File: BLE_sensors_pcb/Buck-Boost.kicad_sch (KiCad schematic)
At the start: 6 parts, among them U3 TPS63031DSK

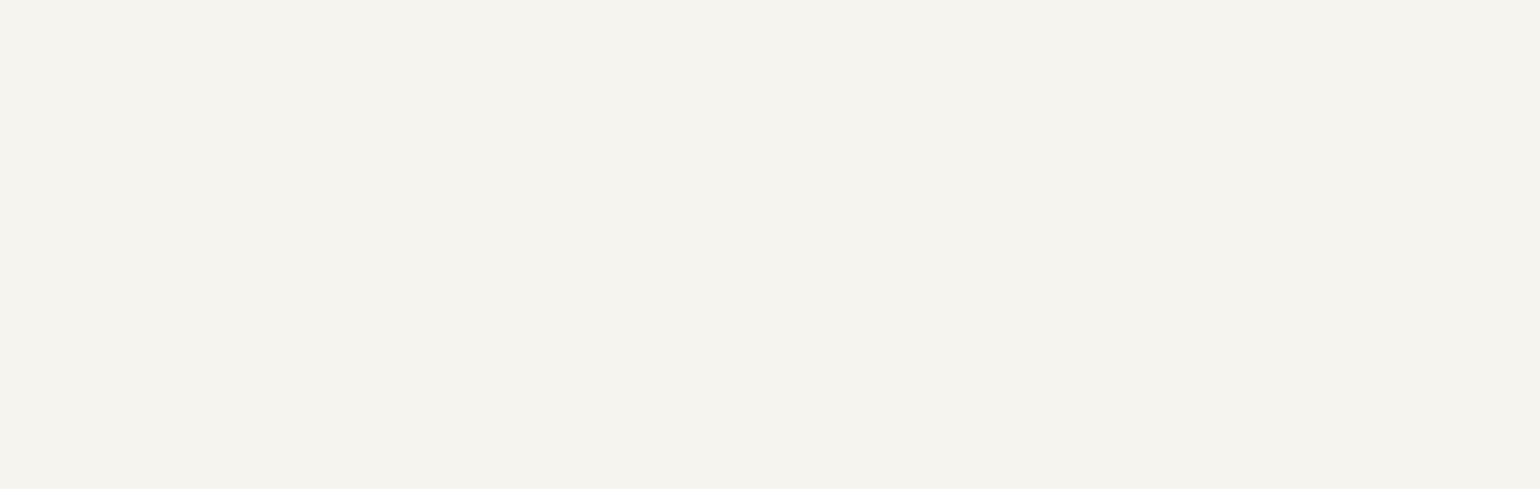
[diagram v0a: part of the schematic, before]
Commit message: Footprints and some pcb placement
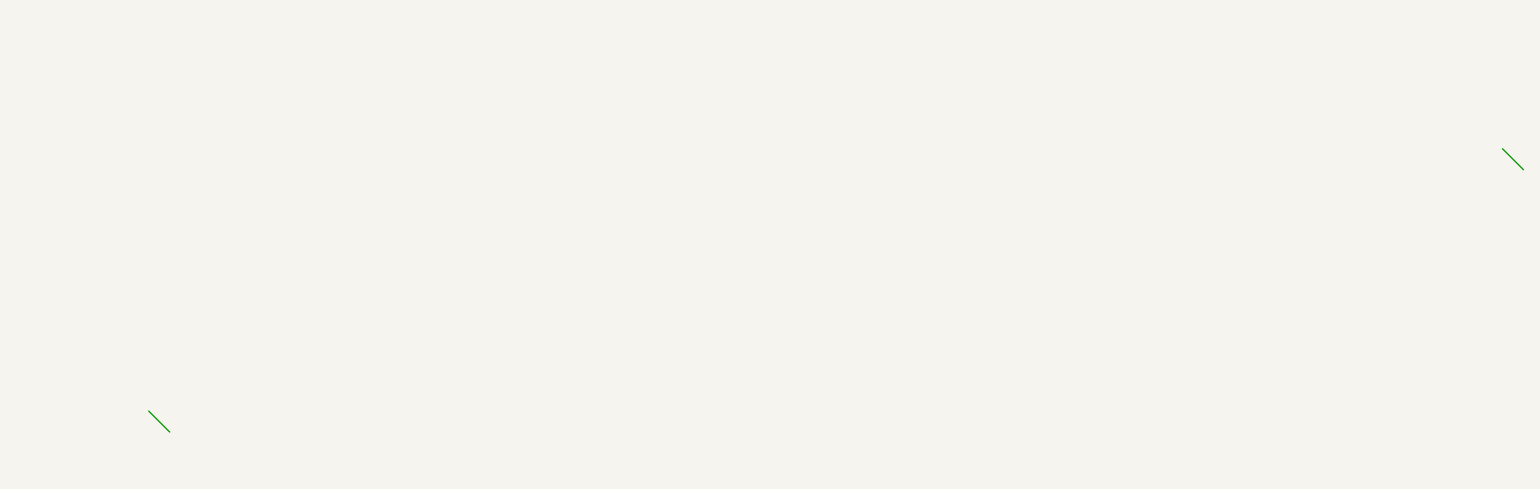
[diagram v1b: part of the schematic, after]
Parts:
- C10, C12, C13: footprint (none) -> Capacitor_SMD:C_0805_2012Metric
- C11: footprint (none) -> Capacitor_SMD:C_0603_1608Metric
- L1: footprint (none) -> Inductor_SMD:L_1210_3225Metric
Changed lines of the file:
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@@
 		(color 0 0 0 0)
+	)
+	(bus_entry
+		(at 224.79 116.84)
+		(size 2.54 2.54)
+		(stroke
+			(width 0)
+			(type default)
+		)
+	)
+	(bus_entry
+		(at 388.62 85.09)
+		(size 2.54 2.54)
+		(stroke
+			(width 0)
+			(type default)
+		)
 	)
 	(wire
@@
 			)
 		)
-		(property "Footprint" ""
+		(property "Footprint" "Capacitor_SMD:C_0603_1608Metric"
 			(at 115.57 99.06 0)
 			(effects
@@
 			)
 		)
-		(property "Footprint" ""
+		(property "Footprint" "Capacitor_SMD:C_0805_2012Metric"
 			(at 107.95 93.98 0)
 			(effects
@@
 			)
 		)
-		(property "Footprint" ""
+		(property "Footprint" "Capacitor_SMD:C_0805_2012Metric"
 			(at 177.8 93.98 0)
 			(effects
@@
 			)
 		)
-		(property "Footprint" ""
+		(property "Footprint" "Inductor_SMD:L_1210_3225Metric"
 			(at 132.08 105.41 0)
 			(effects
@@
 			)
 		)
-		(property "Footprint" ""
+		(property "Footprint" "Capacitor_SMD:C_0805_2012Metric"
 			(at 165.1 93.98 0)
 			(effects

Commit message: save
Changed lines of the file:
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@@
 		(color 0 0 0 0)
-	)
-	(bus_entry
-		(at 224.79 116.84)
-		(size 2.54 2.54)
-		(stroke
-			(width 0)
-			(type default)
-		)
-	)
-	(bus_entry
-		(at 388.62 85.09)
-		(size 2.54 2.54)
-		(stroke
-			(width 0)
-			(type default)
-		)
 	)
 	(wire
